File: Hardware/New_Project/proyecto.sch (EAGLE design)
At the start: 45 parts, among them J1 USB4105-GF-A, Q1 DMP1045U, U1 ESP32C3_QFN32X5, U2 MPU-6050, U3 MCP73831-2ACI/MC, Y1 ABM11W-101-32.0000MHZ-T3

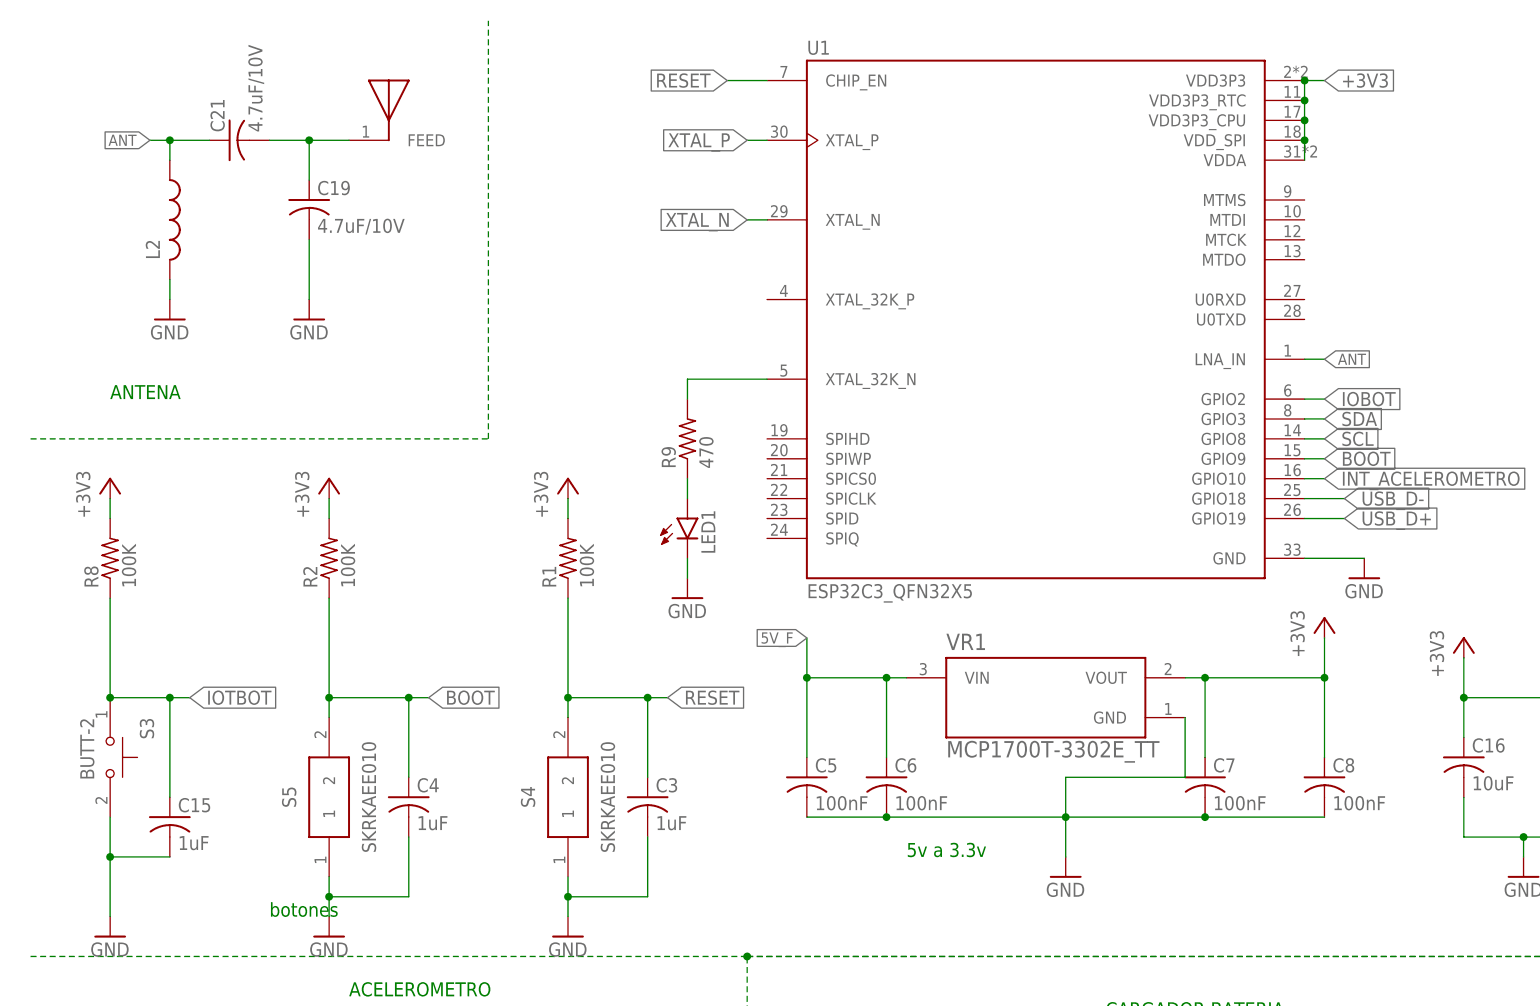
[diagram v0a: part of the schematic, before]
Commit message: Se agrega el diseño corregido
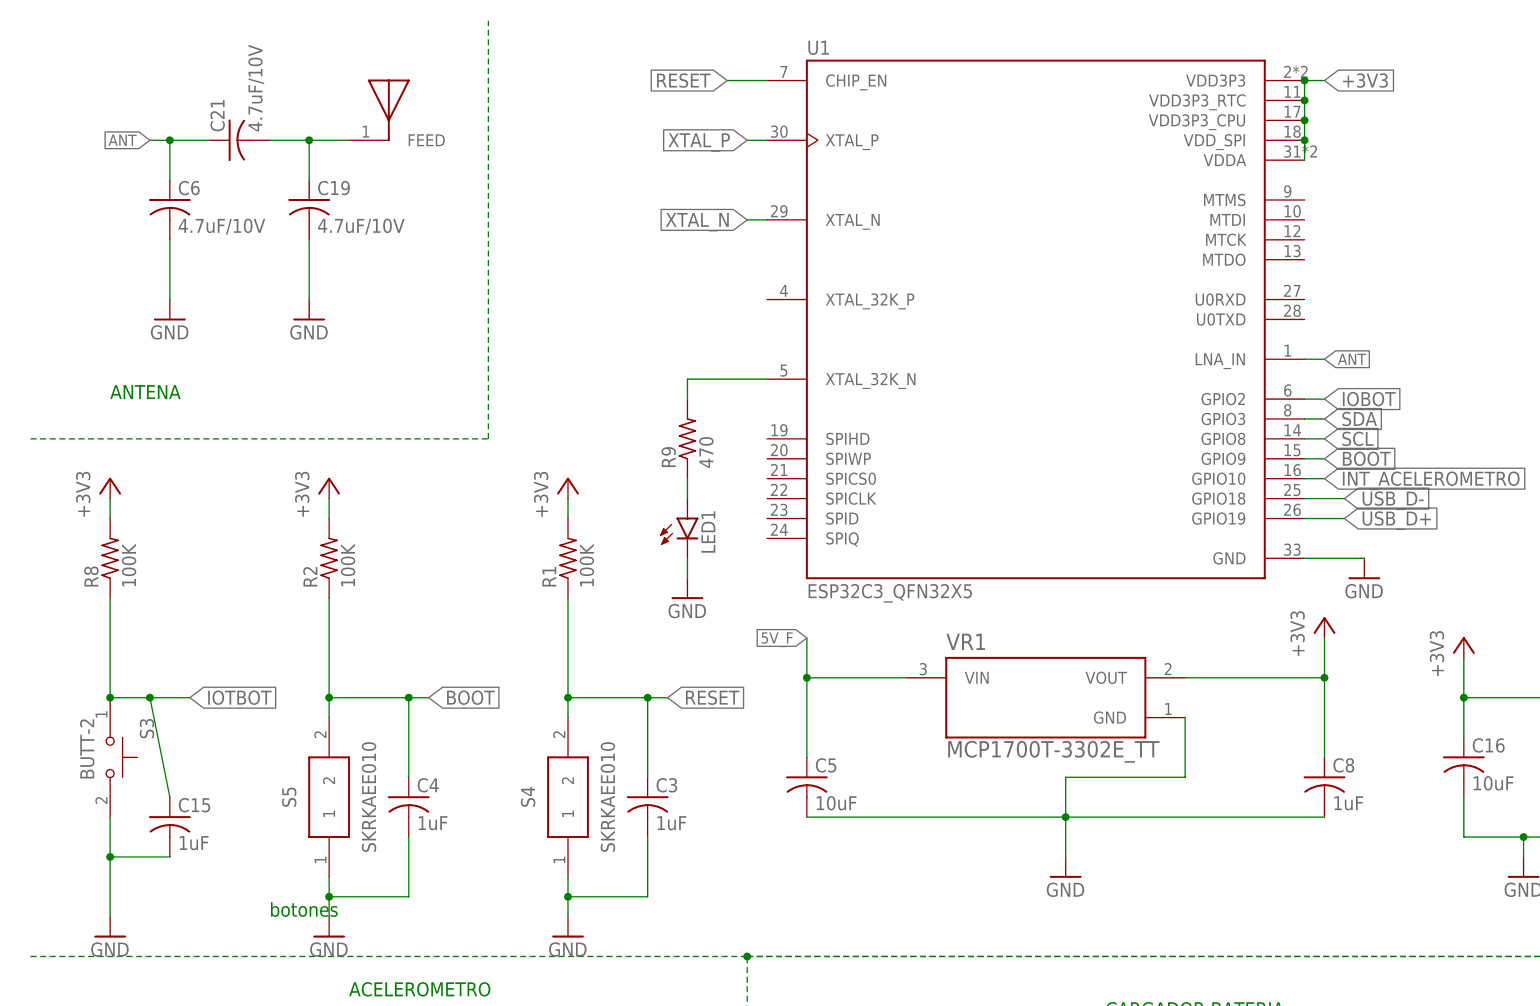
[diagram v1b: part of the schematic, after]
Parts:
- removed C7: 100nF, rcl:C-USC0603
- removed L2: (no value), rcl:L-USL4516C
- C5: value 100nF -> 10uF
- C6: value 100nF -> 4.7uF/10V
- C8: value 100nF -> 1uF
- LED1, LED2: device led:LED -> led:LEDSML0603
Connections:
- net +3V3: no longer C7.1
- net 5V_F: no longer C6.1
- net ANT: now also C6.1; no longer L2.1
- net GND: no longer C7.2, L2.2
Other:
- note removed: "5v a 3.3v"
- moved on the sheet: C6
